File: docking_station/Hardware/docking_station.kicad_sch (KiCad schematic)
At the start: 58 parts, among them IC1 VOM1271T, IC2 VOM1271T, IC3 VOM1271T, IC4 VOM1271T, IC5 VOM1271T, J1 SUPPLY_EN, J2 LIVE_IN, J5 SUPPLY+, J6 SUPPLY-, K1 RELPOL R40N-3021-85-1024, K2 EC2-3NU, K3 EC2-3NU, Q1 SIDR392DP-T1-GE3, Q10 DN2540N8-G, Q11 DN2540N8-G, Q12 2N7002K, Q2 SIDR392DP-T1-GE3, Q3 SIDR392DP-T1-GE3, Q4 SIDR392DP-T1-GE3, Q5 SIDR392DP-T1-GE3, Q6 SIDR392DP-T1-GE3, Q7 SIDR392DP-T1-GE3, Q8 SIDR392DP-T1-GE3, Q9 SIDR392DP-T1-GE3, U1 LTC4357MS8, U2 MCP6561T-E/OT, U3 L78L05AB, U4 ACS712xLCTR-20A, U5 LMV321IYLT, U6 MCP6561T-E/OT

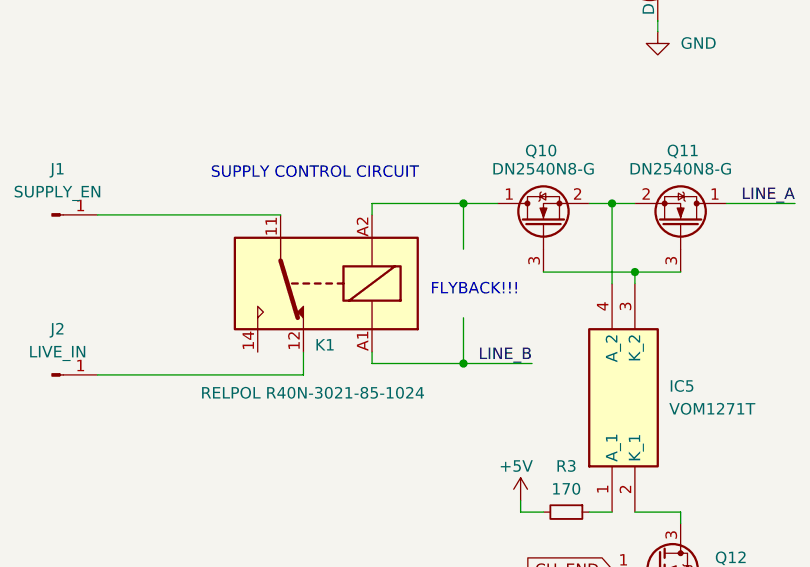
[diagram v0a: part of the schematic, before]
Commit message: schematic complete
snubber parameters set, basic components chosen.
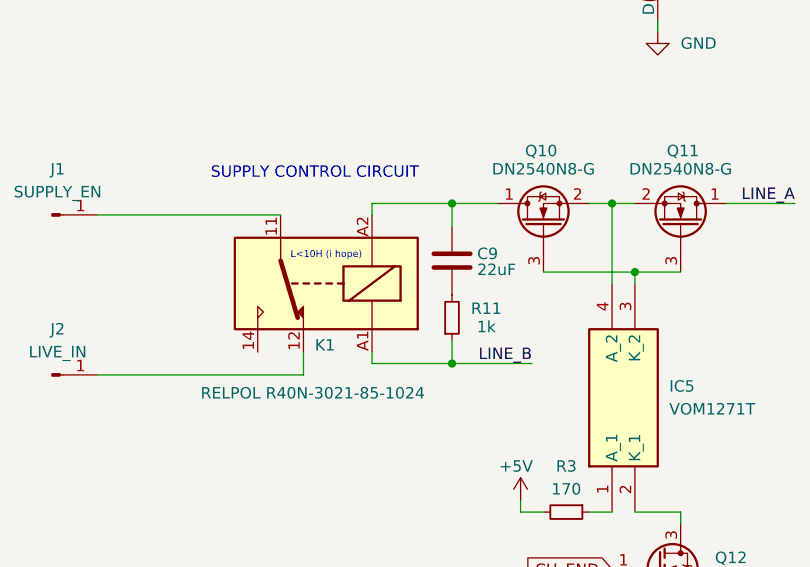
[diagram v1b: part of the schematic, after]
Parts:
- added C9: 22uF, symbol Device:C
- added R11: 1k, symbol Device:R_Small
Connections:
- net LINE_B: now also R11.1
- net at K1.A2, Q10.1 (D): now also C9.1
- new net: C9.2, R11.2
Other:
- note added: "L<10H (i hope)"
- note removed: "FLYBACK!!!"
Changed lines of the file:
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@@
 	)
 	(junction
+		(at 223.52 102.87)
+		(diameter 0)
+		(color 0 0 0 0)
+	)
+	(junction
 		(at 140.97 100.33)
 		(diameter 0)
@@
 	)
 	(junction
+		(at 223.52 120.65)
+		(diameter 0)
+		(color 0 0 0 0)
+	)
+	(junction
 		(at 151.13 111.76)
 		(diameter 0)
@@
 	)
 	(junction
-		(at 224.79 102.87)
-		(diameter 0)
-		(color 0 0 0 0)
-	)
-	(junction
 		(at 95.25 96.52)
 		(diameter 0)
@@
 		(color 0 0 0 0)
 	)
-	(junction
-		(at 224.79 120.65)
-		(diameter 0)
-		(color 0 0 0 0)
-	)
 	(no_connect
 		(at 38.1 175.26)
@@
 	(wire
 		(pts
+			(xy 223.52 102.87) (xy 228.6 102.87)
+		)
+		(stroke
+			(width 0)
+			(type default)
+		)
+	)
+	(wire
+		(pts
 			(xy 115.57 39.37) (xy 125.73 39.37)
 		)
@@
 	(wire
 		(pts
-			(xy 82.55 176.53) (xy 82.55 175.26)
+			(xy 223.52 120.65) (xy 232.41 120.65)
 		)
 		(stroke
@@
 	(wire
 		(pts
-			(xy 224.79 120.65) (xy 224.79 115.57)
+			(xy 82.55 176.53) (xy 82.55 175.26)
 		)
 		(stroke
@@
 	(wire
 		(pts
+			(xy 223.52 118.11) (xy 223.52 120.65)
+		)
+		(stroke
+			(width 0)
+			(type default)
+		)
+	)
+	(wire
+		(pts
 			(xy 102.87 154.94) (xy 107.95 154.94)
 		)
@@
 	(wire
 		(pts
-			(xy 232.41 120.65) (xy 224.79 120.65)
+			(xy 214.63 120.65) (xy 223.52 120.65)
 		)
 		(stroke
@@
 	(wire
 		(pts
-			(xy 214.63 120.65) (xy 224.79 120.65)
-		)
-		(stroke
-			(width 0)
-			(type default)
-		)
-	)
-	(wire
-		(pts
 			(xy 30.48 154.94) (xy 25.4 154.94)
 		)
@@
 	(wire
 		(pts
-			(xy 248.92 138.43) (xy 248.92 137.16)
+			(xy 223.52 102.87) (xy 223.52 105.41)
 		)
 		(stroke
@@
 	(wire
 		(pts
-			(xy 69.85 80.01) (xy 69.85 81.28)
+			(xy 248.92 138.43) (xy 248.92 137.16)
 		)
 		(stroke
@@
 	(wire
 		(pts
-			(xy 67.31 125.73) (xy 74.93 125.73)
+			(xy 69.85 80.01) (xy 69.85 81.28)
 		)
 		(stroke
@@
 	(wire
 		(pts
-			(xy 224.79 102.87) (xy 224.79 107.95)
+			(xy 67.31 125.73) (xy 74.93 125.73)
 		)
 		(stroke
@@
 	(wire
 		(pts
-			(xy 224.79 102.87) (xy 228.6 102.87)
+			(xy 214.63 102.87) (xy 223.52 102.87)
 		)
 		(stroke
@@
 	(wire
 		(pts
-			(xy 224.79 102.87) (xy 214.63 102.87)
-		)
-		(stroke
-			(width 0)
-			(type default)
-		)
-	)
-	(wire
-		(pts
 			(xy 246.38 41.91) (xy 246.38 43.18)
 		)
@@
 		)
 	)
-	(text "FLYBACK!!!"
-		(exclude_from_sim no)
-		(at 226.06 112.522 0)
-		(effects
-			(font
-				(size 1.27 1.27)
-				(color 229 86 0 1)
-			)
-		)
-	)
 	(text "excl. from board"
 		(exclude_from_sim no)
@@
 		)
 	)
+	(text "L<10H (i hope)"
+		(exclude_from_sim no)
+		(at 209.55 108.712 0)
+		(effects
+			(font
+				(size 0.762 0.762)
+			)
+		)
+	)
 	(label "LINE_B"
 		(at 115.57 71.12 0)
@@
 	)
 	(symbol
+		(lib_id "Device:R_Small")
+		(at 223.52 115.57 0)
+		(mirror x)
+		(unit 1)
+		(exclude_from_sim no)
+		(in_bom yes)
+		(on_board yes)
+		(dnp no)
+		(property "Reference" "R11"
+			(at 227.33 114.554 0)
+			(effects
+				(font
+					(size 1.27 1.27)
+				)
+			)
+		)
+		(property "Value" "1k"
+			(at 227.33 116.586 0)
+			(effects
+				(font
+					(size 1.27 1.27)
+				)
+			)
+		)
+		(property "Footprint" ""
+			(at 223.52 115.57 0)
+			(effects
+				(font
+					(size 1.27 1.27)
+				)
+				(hide yes)
+			)
+		)
+		(property "Datasheet" "~"
+			(at 223.52 115.57 0)
+			(effects
+				(font
+					(size 1.27 1.27)
+				)
+				(hide yes)
+			)
+		)
+		(property "Description" "Resistor, small symbol"
+			(at 223.52 115.57 0)
+			(effects
+				(font
+					(size 1.27 1.27)
+				)
+				(hide yes)
+			)
+		)
+		(pin "1"
+		)
+		(pin "2"
+		)
+		(instances
+			(project "docking_station"
+				(path "/08748f9a-6084-44ea-8855-9d9812e8dfdd"
+					(reference "R11")
+					(unit 1)
+				)
+			)
+		)
+	)
+	(symbol
 		(lib_id "Device:Q_NMOS_Depletion_DSG")
 		(at 233.68 105.41 90)
@@
 					(unit 1)
 				)
+			)
+		)
+	)
+	(symbol
+		(lib_id "Device:C")
+		(at 223.52 109.22 0)
+		(unit 1)
+		(exclude_from_sim no)
+		(in_bom yes)
+		(on_board yes)
+		(dnp no)
+		(property "Reference" "C9"
+			(at 226.314 108.458 0)
+			(effects
+				(font
+					(size 1.27 1.27)
+				)
+				(justify left)
+			)
+		)
+		(property "Value" "22uF"
+			(at 226.314 110.236 0)
+			(effects
+				(font
+					(size 1.27 1.27)
+				)
+				(justify left)
+			)
+		)
+		(property "Footprint" ""
+			(at 224.4852 113.03 0)
+			(effects
+				(font
+					(size 1.27 1.27)
+				)
+				(hide yes)
+			)
+		)
+		(property "Datasheet" "~"
+			(at 223.52 109.22 0)
+			(effects
+				(font
+					(size 1.27 1.27)
+				)
+				(hide yes)
+			)
+		)
+		(property "Description" "Unpolarized capacitor"
+			(at 223.52 109.22 0)
+			(effects
+				(font
+					(size 1.27 1.27)
+				)
+				(hide yes)
+			)
+		)
+		(pin "2"
+		)
+		(pin "1"
+		)
+		(instances
+			(project ""
+				(path "/08748f9a-6084-44ea-8855-9d9812e8dfdd"
+					(reference "C9")
+					(unit 1)
+				)

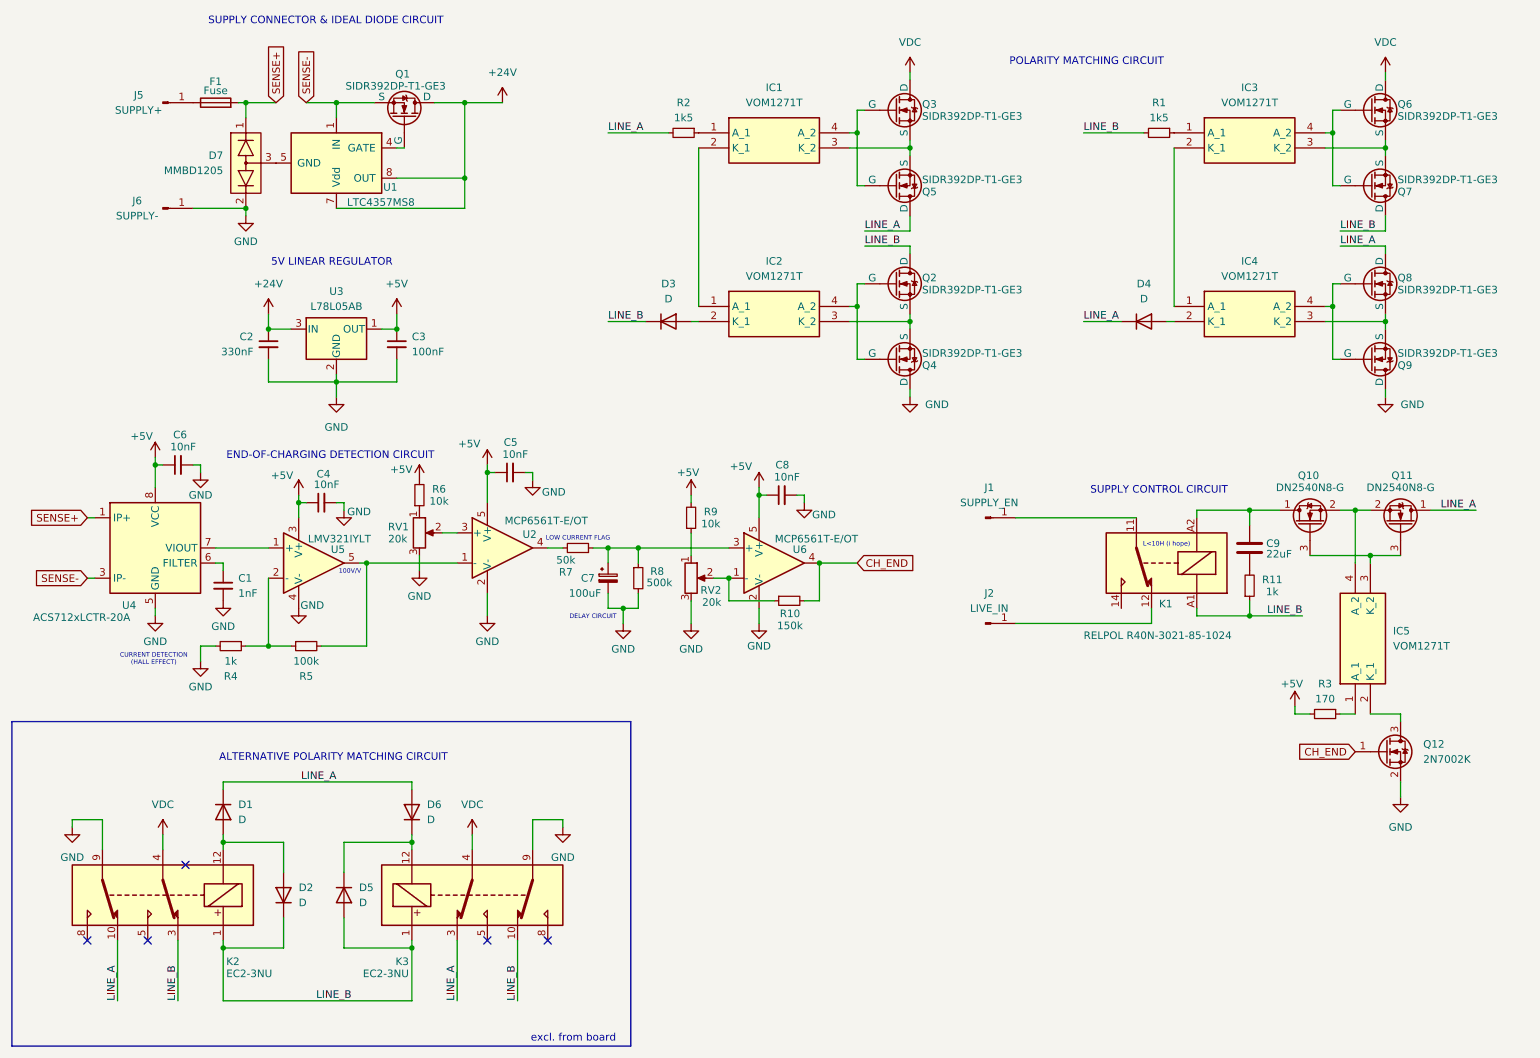
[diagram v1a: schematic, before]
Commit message: assigned stock footprints
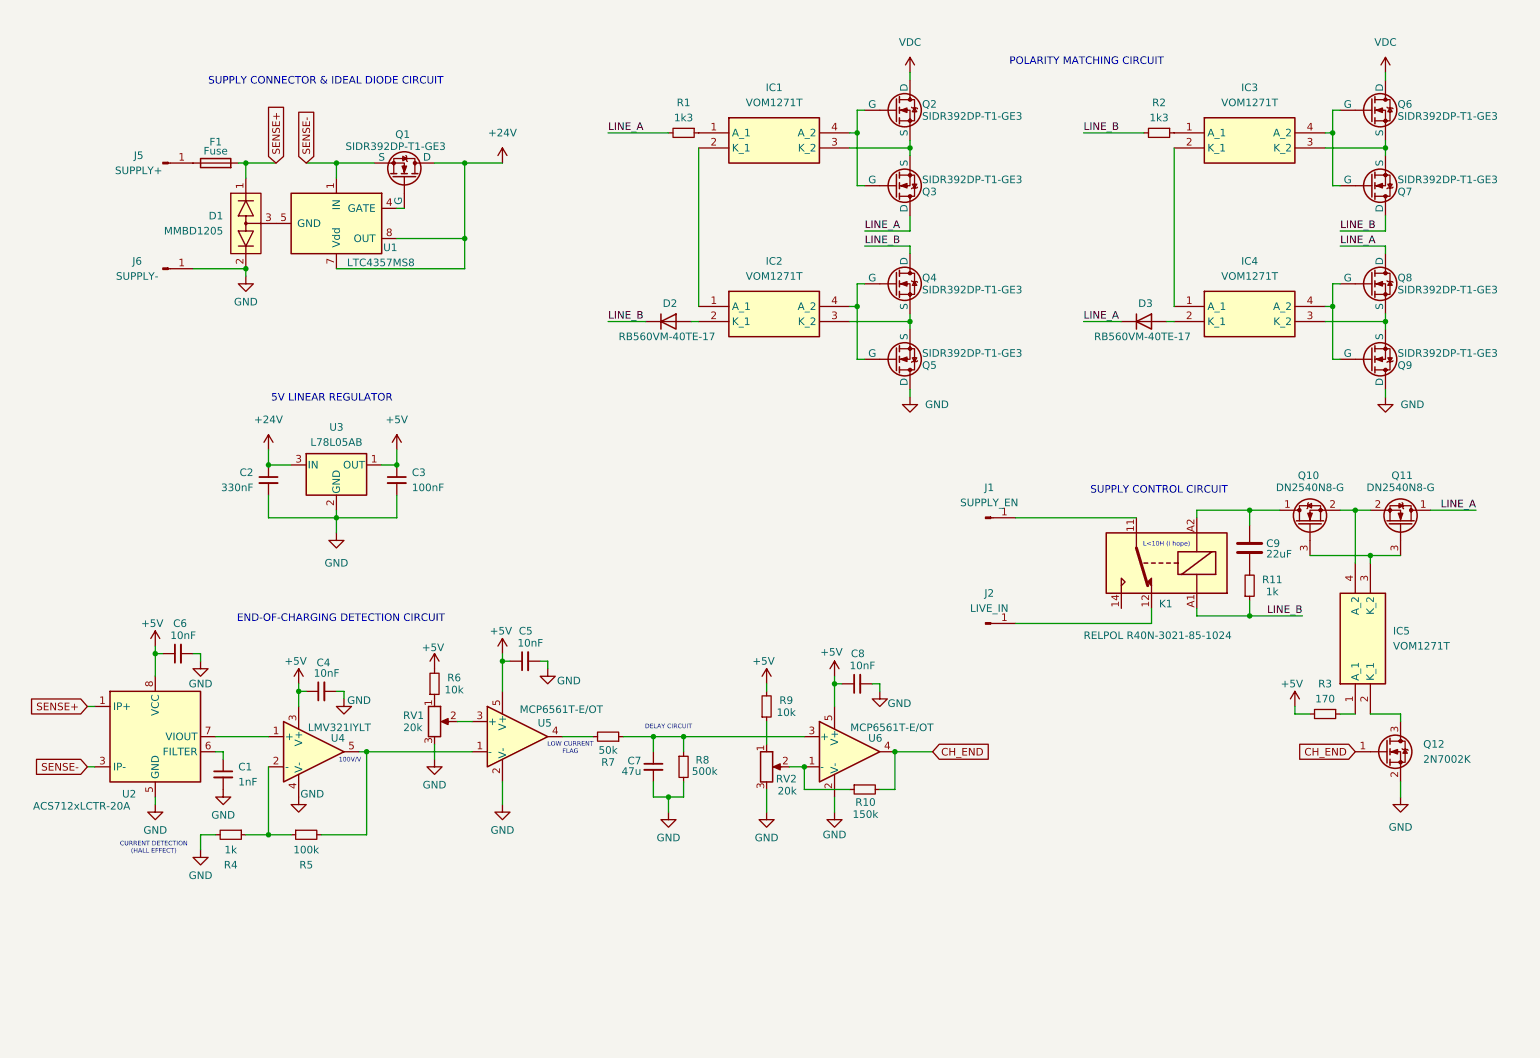
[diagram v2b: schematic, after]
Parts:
- removed C7: 100uF, symbol Device:C_Polarized_Small
- removed D1, D2, D4, D5, D6: D, symbol Device:D
- removed K2, K3: EC2-3NU, Relay_THT:Relay_DPDT_Kemet_EC2, symbol Relay:EC2-3NU
- added C7: 47u, Capacitor_SMD:C_1206_3216Metric, symbol Device:C_Small
- added D3: RB560VM-40TE-17, Diode_SMD:D_SOD-323F, symbol Device:D
- C1, C2, C3, C4, C5, C6, C8: footprint (none) -> Capacitor_SMD:C_0805_2012Metric
- C9: footprint (none) -> Capacitor_SMD:C_2220_5750Metric
- D2: renamed from D3; value D -> RB560VM-40TE-17; footprint (none) -> Diode_SMD:D_SOD-323F
- Q10, Q11: footprint (none) -> Package_TO_SOT_SMD:SOT-89-3
- R1: renamed from R2; value 1k5 -> 1k3
- R10, R4, R5, R6, R7, R8, R9: footprint (none) -> Resistor_SMD:R_0402_1005Metric
- R2: renamed from R1; value 1k5 -> 1k3
- R3: footprint (none) -> Resistor_SMD:R_0805_2012Metric
- renumbered D7 to D1, Q3 to Q2, Q5 to Q3, Q2 to Q4, Q4 to Q5, U4 to U2, U5 to U4, U2 to U5
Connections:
- net GND: now also C7.2
- net LINE_A: now also D3.1 (K)
- net at R7.1, R8.1, U6.3 (+): now also C7.1
- net at IC4.2 (K_1): now also D3.2 (A)
- no-connect marks 5 -> 0
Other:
- note removed: "ALTERNATIVE POLARITY MATCHING CIRCUIT"
- note removed: "excl. from board"
- moved on the sheet: C1, C2, C3, C4, C5, C6, C8, D1, F1, J5, J6, Q1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

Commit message: schematic v1.0. added gitignore
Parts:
- removed J1: SUPPLY_EN, symbol Connector:Conn_01x01_Pin
- removed J2: LIVE_IN, symbol Connector:Conn_01x01_Pin
- added J1: WAGO, symbol Connector_Generic:Conn_01x02
- added J2: XT60, symbol Connector_Generic:Conn_01x02
- added J3: Conn_01x05_Pin, symbol Connector:Conn_01x05_Pin
- added JP1: Jumper_2_Small_Bridged, symbol Jumper:Jumper_2_Small_Bridged
- added TP1, TP10, TP11, TP12, TP13, TP14, TP15, TP16, TP17, TP18, TP19, TP2, TP20, TP21, TP22, TP3, TP4, TP5, TP6, TP7, TP8, TP9: TestPoint, symbol Connector:TestPoint
- added TP23: TestPoint_2Pole, symbol Connector:TestPoint_2Pole
- IC1, IC2, IC3, IC4, IC5: footprint SOP254P675X240-4N -> firo_footprints:SOP254P675X240-4N
- K1: footprint Relay_THT:Relay_SPDT_Fujitsu_FTR-LYCA005x_FormC_Vertical -> firo_footprints:Relpol R40N
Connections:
- net +24V: now also TP1.1
- net +5V: now also J3.1 (Pin_1), TP2.1
- net CH_END: now also J3.4 (Pin_4), JP1.2 (B); no longer R10.2, U6.4
- net GND: now also J3.5 (Pin_5), TP20.1, TP21.1, TP22.1
- net LINE_A: now also J2.1 (Pin_1), TP3.1
- net LINE_B: now also J2.2 (Pin_2), TP4.1
- net SENSE+: now also TP23.2
- net SENSE-: now also TP23.1
- net at IC3.3 (K_2), Q6.1 (S), Q7.1 (S): now also TP17.1
- net at IC3.4 (A_2), Q6.2 (G), Q7.2 (G): now also TP13.1
- net at IC4.3 (K_2), Q8.1 (S), Q9.1 (S): now also TP18.1
- net at IC4.4 (A_2), Q8.2 (G), Q9.2 (G): now also TP14.1
- net at C9.1, K1.A2, Q10.1 (D): now also TP10.1
- net at K1.11: now also J1.2 (Pin_2)
- net at F1.1, J5.1 (Pin_1): now also TP19.1
- net at IC2.3 (K_2), Q4.1 (S), Q5.1 (S): now also TP16.1
- net at IC2.4 (A_2), Q4.2 (G), Q5.2 (G): now also TP12.1
- net at C7.1, R7.1, R8.1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: now also TP8.1
- net at R7.2, U5.4: now also TP7.1
- net at IC1.3 (K_2), Q2.1 (S), Q3.1 (S): now also TP15.1
- net at IC1.4 (A_2), Q2.2 (G), Q3.2 (G): now also TP11.1
- net AMP_OUT: now reaches R5.2, U4.5, U5.1 (-)
- net AMP_OUT: now also J3.3 (Pin_3), TP6.1
- net CS_VOUT: now reaches U2.7 (VIOUT), U4.1 (+)
- net CS_VOUT: now also J3.2 (Pin_2), TP5.1
- net at K1.14: now also J1.1 (Pin_1)
- new net: JP1.1 (A), R10.2, TP9.1, U6.4
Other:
- note added: "BYPASS JMP"
- note added: "EOC BYPASS CONNECTOR"
- note added: "LIVE_IN"
- note added: "LOW CURR. FLAG"
- note added: "PAD CONNECTOR"
- note added: "SOLDERED"
- note added: "SUPPLY"
- note added: "TEST POINTS"
- note removed: "LOW CURRENT FLAG"
- title: (none) -> Charging Station Controller for FIRO rover
- moved on the sheet: C1, C2, C3, C4, C5, C6, C7, C8, J5, J6, R10, R4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

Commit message: more footprints created & assigned
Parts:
- J2: footprint (none) -> Connector_AMASS:AMASS_XT60PW-F_1x02_P7.20mm_Horizontal
- J3: footprint (none) -> Connector_PinHeader_2.54mm:PinHeader_1x05_P2.54mm_Vertical
- JP1: footprint (none) -> Jumper:SolderJumper-2_P1.3mm_Bridged2Bar_RoundedPad1.0x1.5mm
- R1, R11, R2: footprint (none) -> Resistor_SMD:R_1206_3216Metric
- RV1, RV2: footprint (none) -> firo_footprints:BOURNS_3313J-1_SMD
- TP1, TP10, TP11, TP12, TP13, TP14, TP15, TP16, TP17, TP18, TP19, TP2, TP3, TP4, TP5, TP6, TP7, TP8, TP9: footprint (none) -> TestPoint:TestPoint_Pad_D2.0mm
- TP20, TP21, TP22: footprint (none) -> TestPoint:TestPoint_Bridge_Pitch3.81mm_Drill1.3mm
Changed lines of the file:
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@@
 			)
 		)
-		(property "Footprint" ""
+		(property "Footprint" "TestPoint:TestPoint_Bridge_Pitch3.81mm_Drill1.3mm"
 			(at 52.07 171.45 0)
 			(effects
@@
 			)
 		)
-		(property "Footprint" ""
+		(property "Footprint" "TestPoint:TestPoint_Pad_D2.0mm"
 			(at 162.56 64.77 0)
 			(effects
@@
 			)
 		)
-		(property "Footprint" ""
+		(property "Footprint" "Resistor_SMD:R_1206_3216Metric"
 			(at 223.52 115.57 0)
 			(effects
@@
 			)
 		)
-		(property "Footprint" ""
+		(property "Footprint" "TestPoint:TestPoint_Pad_D2.0mm"
 			(at 166.37 76.2 0)
 			(effects
@@
 			)
 		)
-		(property "Footprint" ""
+		(property "Footprint" "Connector_PinHeader_2.54mm:PinHeader_1x05_P2.54mm_Vertical"
 			(at 135.89 175.26 0)
 			(effects
@@
 			)
 		)
-		(property "Footprint" ""
+		(property "Footprint" "TestPoint:TestPoint_Pad_D2.0mm"
 			(at 246.38 46.99 0)
 			(effects
@@
 			)
 		)
-		(property "Footprint" ""
+		(property "Footprint" "TestPoint:TestPoint_Pad_D2.0mm"
 			(at 146.05 132.08 0)
 			(effects
@@
 			)
 		)
-		(property "Footprint" ""
+		(property "Footprint" "TestPoint:TestPoint_Pad_D2.0mm"
 			(at 167.64 134.62 0)
 			(effects
@@
 			)
 		)
-		(property "Footprint" ""
+		(property "Footprint" "Resistor_SMD:R_1206_3216Metric"
 			(at 208.28 39.37 0)
 			(effects
@@
 			)
 		)
-		(property "Footprint" ""
+		(property "Footprint" "TestPoint:TestPoint_Pad_D2.0mm"
 			(at 38.1 182.88 0)
 			(effects
@@
 			)
 		)
-		(property "Footprint" ""
+		(property "Footprint" "TestPoint:TestPoint_Bridge_Pitch3.81mm_Drill1.3mm"
 			(at 58.42 171.45 0)
 			(effects
@@
 			)
 		)
-		(property "Footprint" ""
+		(property "Footprint" "TestPoint:TestPoint_Pad_D2.0mm"
 			(at 68.58 132.08 0)
 			(effects
@@
 			)
 		)
-		(property "Footprint" ""
+		(property "Footprint" "TestPoint:TestPoint_Pad_D2.0mm"
 			(at 242.57 35.56 0)
 			(effects
@@
 			)
 		)
-		(property "Footprint" ""
+		(property "Footprint" "TestPoint:TestPoint_Pad_D2.0mm"
 			(at 111.76 132.08 0)
 			(effects
@@
 			)
 		)
-		(property "Footprint" ""
+		(property "Footprint" "firo_footprints:BOURNS_3313J-1_SMD"
 			(at 147.32 137.16 0)
 			(effects
@@
 			)
 		)
-		(property "Footprint" ""
+		(property "Footprint" "TestPoint:TestPoint_Pad_D2.0mm"
 			(at 92.71 134.62 0)
 			(effects
@@
 			)
 		)
-		(property "Footprint" ""
+		(property "Footprint" "Connector_AMASS:AMASS_XT60PW-F_1x02_P7.20mm_Horizontal"
 			(at 161.29 175.26 0)
 			(effects
@@
 			)
 		)
-		(property "Footprint" ""
+		(property "Footprint" "firo_footprints:BOURNS_3313J-1_SMD"
 			(at 91.44 129.54 0)
 			(effects
@@
 			)
 		)
-		(property "Footprint" ""
+		(property "Footprint" "TestPoint:TestPoint_Pad_D2.0mm"
 			(at 29.21 170.18 0)
 			(effects
@@
 			)
 		)
-		(property "Footprint" ""
+		(property "Footprint" "TestPoint:TestPoint_Pad_D2.0mm"
 			(at 228.6 102.87 0)
 			(effects
@@
 			)
 		)
-		(property "Footprint" ""
+		(property "Footprint" "TestPoint:TestPoint_Pad_D2.0mm"
 			(at 162.56 35.56 0)
 			(effects
@@
 			)
 		)
-		(property "Footprint" ""
+		(property "Footprint" "Resistor_SMD:R_1206_3216Metric"
 			(at 128.27 39.37 0)
 			(effects
@@
 			)
 		)
-		(property "Footprint" ""
+		(property "Footprint" "TestPoint:TestPoint_Bridge_Pitch3.81mm_Drill1.3mm"
 			(at 45.72 171.45 0)
 			(effects
@@
 			)
 		)
-		(property "Footprint" ""
+		(property "Footprint" "TestPoint:TestPoint_Pad_D2.0mm"
 			(at 49.53 44.45 0)
 			(effects
@@
 			)
 		)
-		(property "Footprint" ""
+		(property "Footprint" "TestPoint:TestPoint_Pad_D2.0mm"
 			(at 31.75 182.88 0)
 			(effects
@@
 			)
 		)
-		(property "Footprint" ""
+		(property "Footprint" "Jumper:SolderJumper-2_P1.3mm_Bridged2Bar_RoundedPad1.0x1.5mm"
 			(at 179.07 134.62 0)
 			(effects
@@
 			)
 		)
-		(property "Footprint" ""
+		(property "Footprint" "TestPoint:TestPoint_Pad_D2.0mm"
 			(at 166.37 46.99 0)
 			(effects
@@
 			)
 		)
-		(property "Footprint" ""
+		(property "Footprint" "TestPoint:TestPoint_Pad_D2.0mm"
 			(at 246.38 76.2 0)
 			(effects
@@
 			)
 		)
-		(property "Footprint" ""
+		(property "Footprint" "TestPoint:TestPoint_Pad_D2.0mm"
 			(at 242.57 64.77 0)
 			(effects
@@
 			)
 		)
-		(property "Footprint" ""
+		(property "Footprint" "TestPoint:TestPoint_Pad_D2.0mm"
 			(at 22.86 170.18 0)
 			(effects

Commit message: something
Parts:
- added TP24, TP25: TestPoint, TestPoint:TestPoint_Bridge_Pitch3.81mm_Drill1.3mm, symbol Connector:TestPoint
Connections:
- net LINE_A: now also TP24.1
- net LINE_B: now also TP25.1
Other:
- moved on the sheet: J3
